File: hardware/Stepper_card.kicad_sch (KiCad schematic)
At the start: 2 parts, among them J3 PCIE-036-02-X-D-TH

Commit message: more routing
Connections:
- net +3V3: now also J3.A11, J3.B11; no longer J3.A12, J3.B12
- net CIPO: now also J3.A5, J3.B5; no longer J3.A3
- net COPI: now also J3.B4
- net SCL: now also J3.B8
- net SCLK: now also J3.A3, J3.B3; no longer J3.A5
- net SDA: now also J3.B7
- net VM: now also J3.A12, J3.B12
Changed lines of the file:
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@@
+	)
+	(junction
+		(at 119.38 104.14)
+		(diameter 0)
+		(color 0 0 0 0)
 	)
 	(junction
@@
 	)
 	(junction
+		(at 163.83 104.14)
+		(diameter 0)
+		(color 0 0 0 0)
+	)
+	(junction
 		(at 172.72 99.06)
 		(diameter 0)
@@
 	(wire
 		(pts
+			(xy 163.83 104.14) (xy 163.83 106.68)
+		)
+		(stroke
+			(width 0)
+			(type default)
+		)
+	)
+	(wire
+		(pts
 			(xy 119.38 114.3) (xy 119.38 116.84)
 		)
@@
 	(wire
 		(pts
+			(xy 157.48 101.6) (xy 196.85 101.6)
+		)
+		(stroke
+			(width 0)
+			(type default)
+		)
+	)
+	(wire
+		(pts
 			(xy 163.83 119.38) (xy 163.83 124.46)
 		)
@@
 	(wire
 		(pts
-			(xy 132.08 104.14) (xy 125.73 104.14)
-		)
-		(stroke
-			(width 0)
-			(type default)
-		)
-	)
-	(wire
-		(pts
 			(xy 132.08 116.84) (xy 119.38 116.84)
 		)
@@
 	(wire
 		(pts
+			(xy 119.38 104.14) (xy 132.08 104.14)
+		)
+		(stroke
+			(width 0)
+			(type default)
+		)
+	)
+	(wire
+		(pts
 			(xy 157.48 83.82) (xy 196.85 83.82)
 		)
@@
 	(wire
 		(pts
-			(xy 157.48 104.14) (xy 196.85 104.14)
-		)
-		(stroke
-			(width 0)
-			(type default)
-		)
-	)
-	(wire
-		(pts
 			(xy 119.38 106.68) (xy 119.38 104.14)
 		)
@@
 	(wire
 		(pts
+			(xy 125.73 81.28) (xy 132.08 81.28)
+		)
+		(stroke
+			(width 0)
+			(type default)
+		)
+	)
+	(wire
+		(pts
 			(xy 196.85 121.92) (xy 181.61 121.92)
 		)
@@
 	(wire
 		(pts
+			(xy 132.08 101.6) (xy 125.73 101.6)
+		)
+		(stroke
+			(width 0)
+			(type default)
+		)
+	)
+	(wire
+		(pts
+			(xy 125.73 83.82) (xy 132.08 83.82)
+		)
+		(stroke
+			(width 0)
+			(type default)
+		)
+	)
+	(wire
+		(pts
 			(xy 157.48 78.74) (xy 196.85 78.74)
 		)
@@
 	(wire
 		(pts
+			(xy 119.38 104.14) (xy 119.38 101.6)
+		)
+		(stroke
+			(width 0)
+			(type default)
+		)
+	)
+	(wire
+		(pts
 			(xy 157.48 91.44) (xy 196.85 91.44)
 		)
@@
 	(wire
 		(pts
-			(xy 163.83 106.68) (xy 196.85 106.68)
+			(xy 163.83 104.14) (xy 196.85 104.14)
+		)
+		(stroke
+			(width 0)
+			(type default)
+		)
+	)
+	(wire
+		(pts
+			(xy 157.48 104.14) (xy 163.83 104.14)
 		)
 		(stroke
@@
 	(wire
 		(pts
+			(xy 125.73 93.98) (xy 132.08 93.98)
+		)
+		(stroke
+			(width 0)
+			(type default)
+		)
+	)
+	(wire
+		(pts
+			(xy 125.73 91.44) (xy 132.08 91.44)
+		)
+		(stroke
+			(width 0)
+			(type default)
+		)
+	)
+	(wire
+		(pts
 			(xy 172.72 99.06) (xy 172.72 110.49)
 		)
@@
 			(width 0)
 			(type default)
+		)
+	)
+	(wire
+		(pts
+			(xy 125.73 86.36) (xy 132.08 86.36)
+		)
+		(stroke
+			(width 0)
+			(type default)
+		)
+	)
+	(label "SCLK"
+		(at 163.83 81.28 180)
+		(effects
+			(font
+				(size 1.27 1.27)
+			)
+			(justify right bottom)
+		)
+	)
+	(label "SCLK"
+		(at 125.73 81.28 0)
+		(effects
+			(font
+				(size 1.27 1.27)
+			)
+			(justify left bottom)
+		)
+	)
+	(label "CIPO"
+		(at 125.73 86.36 0)
+		(effects
+			(font
+				(size 1.27 1.27)
+			)
+			(justify left bottom)
+		)
+	)
+	(label "SCL"
+		(at 125.73 93.98 0)
+		(effects
+			(font
+				(size 1.27 1.27)
+			)
+			(justify left bottom)
+		)
+	)
+	(label "COPI"
+		(at 125.73 83.82 0)
+		(effects
+			(font
+				(size 1.27 1.27)
+			)
+			(justify left bottom)
 		)
 	)
@@
 		)
 	)
-	(label "CIPO"
-		(at 163.83 81.28 180)
-		(effects
-			(font
-				(size 1.27 1.27)
-			)
-			(justify right bottom)
-		)
-	)
 	(label "DIR"
 		(at 163.83 78.74 180)
@@
 		)
 	)
+	(label "SDA"
+		(at 125.73 91.44 0)
+		(effects
+			(font
+				(size 1.27 1.27)
+			)
+			(justify left bottom)
+		)
+	)
 	(label "VM"
-		(at 163.83 106.68 180)
+		(at 163.83 104.14 180)
 		(effects
 			(font
@@
 		)
 	)
-	(label "SCLK"
-		(at 163.83 86.36 180)
-		(effects
-			(font
-				(size 1.27 1.27)
-			)
-			(justify right bottom)
-		)
-	)
 	(label "STEP"
 		(at 163.83 76.2 180)
@@
 	)
 	(label "+3V3"
-		(at 163.83 104.14 180)
+		(at 163.83 101.6 180)
 		(effects
 			(font
@@
 		)
 	)
-	(hierarchical_label "CIPO"
-		(shape input)
-		(at 196.85 81.28 0)
-		(effects
-			(font
-				(size 1.27 1.27)
-			)
-			(justify left)
+	(label "CIPO"
+		(at 163.83 86.36 180)
+		(effects
+			(font
+				(size 1.27 1.27)
+			)
+			(justify right bottom)
 		)
 	)
@@
 	(hierarchical_label "SCLK"
 		(shape input)
+		(at 196.85 81.28 0)
+		(effects
+			(font
+				(size 1.27 1.27)
+			)
+			(justify left)
+		)
+	)
+	(hierarchical_label "CIPO"
+		(shape input)
 		(at 196.85 86.36 0)
 		(effects
@@
 		)
 	)
-	(hierarchical_label "+3V3"
-		(shape input)
-		(at 196.85 104.14 0)
-		(effects
-			(font
-				(size 1.27 1.27)
-			)
-			(justify left)
-		)
-	)
 	(hierarchical_label "GND"
 		(shape input)
@@
 		)
 	)
+	(hierarchical_label "+3V3"
+		(shape input)
+		(at 196.85 101.6 0)
+		(effects
+			(font
+				(size 1.27 1.27)
+			)
+			(justify left)
+		)
+	)
 	(hierarchical_label "VM"
 		(shape input)
-		(at 196.85 106.68 0)
+		(at 196.85 104.14 0)
 		(effects
 			(font
@@
 	(symbol
 		(lib_id "power:+3V3")
-		(at 119.38 104.14 0)
+		(at 119.38 101.6 0)
 		(mirror y)
 		(unit 1)
@@
 		(fields_autoplaced yes)
 		(property "Reference" "#PWR022"
-			(at 119.38 107.95 0)
+			(at 119.38 105.41 0)
 			(effects
 				(font
@@
 		)
 		(property "Value" "VM"
-			(at 119.38 99.06 0)
+			(at 119.38 96.52 0)
 			(effects
 				(font
@@
 		)
 		(property "Footprint" ""
-			(at 119.38 104.14 0)
+			(at 119.38 101.6 0)
 			(effects
 				(font
@@
 		)
 		(property "Datasheet" ""
-			(at 119.38 104.14 0)
+			(at 119.38 101.6 0)
 			(effects
 				(font
@@
 		)
 		(property "Description" "Power symbol creates a global label with name \"+3V3\""
-			(at 119.38 104.14 0)
+			(at 119.38 101.6 0)
 			(effects
 				(font
@@
 	(symbol
 		(lib_id "power:+3V3")
-		(at 125.73 104.14 0)
+		(at 125.73 101.6 0)
 		(mirror y)
 		(unit 1)
@@
 		(fields_autoplaced yes)
 		(property "Reference" "#PWR024"
-			(at 125.73 107.95 0)
+			(at 125.73 105.41 0)
 			(effects
 				(font
@@
 		)
 		(property "Value" "+3V3"
-			(at 125.73 99.06 0)
+			(at 125.73 96.52 0)
 			(effects
 				(font
@@
 		)
 		(property "Footprint" ""
-			(at 125.73 104.14 0)
+			(at 125.73 101.6 0)
 			(effects
 				(font
@@
 		)
 		(property "Datasheet" ""
-			(at 125.73 104.14 0)
+			(at 125.73 101.6 0)
 			(effects
 				(font
@@
 		)
 		(property "Description" "Power symbol creates a global label with name \"+3V3\""
-			(at 125.73 104.14 0)
+			(at 125.73 101.6 0)
 			(effects
 				(font
@@
 			(project "BREAD_Slice"
 				(path "/66043bca-a260-4915-9fce-8a51d324c687/d8306a08-064c-4eaa-a20b-e93bd3d278a4"
-					(reference "#PWR045")
+					(reference "#PWR0103")
 					(unit 1)
 				)
@@
 				)
 				(path "/66043bca-a260-4915-9fce-8a51d324c687/f5513ef3-0e61-46f0-9947-38308ddef54a"
-					(reference "#PWR031")
+					(reference "#PWR0101")
 					(unit 1)
 				)
 				(path "/66043bca-a260-4915-9fce-8a51d324c687/f619a8b7-4532-47fb-ad5f-06ccb6ce9665"
-					(reference "#PWR038")
-					(unit 1)
-				)
+					(reference "#PWR0102")
+					(unit 1)
+				)

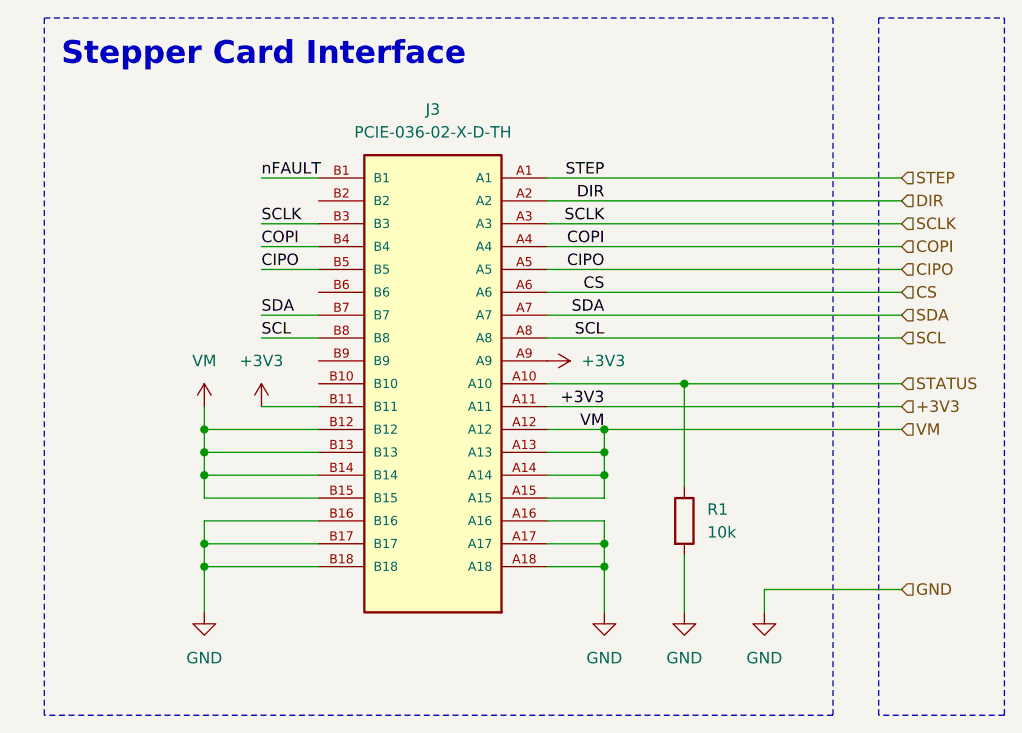
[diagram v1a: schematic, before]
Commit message: finished initial routing
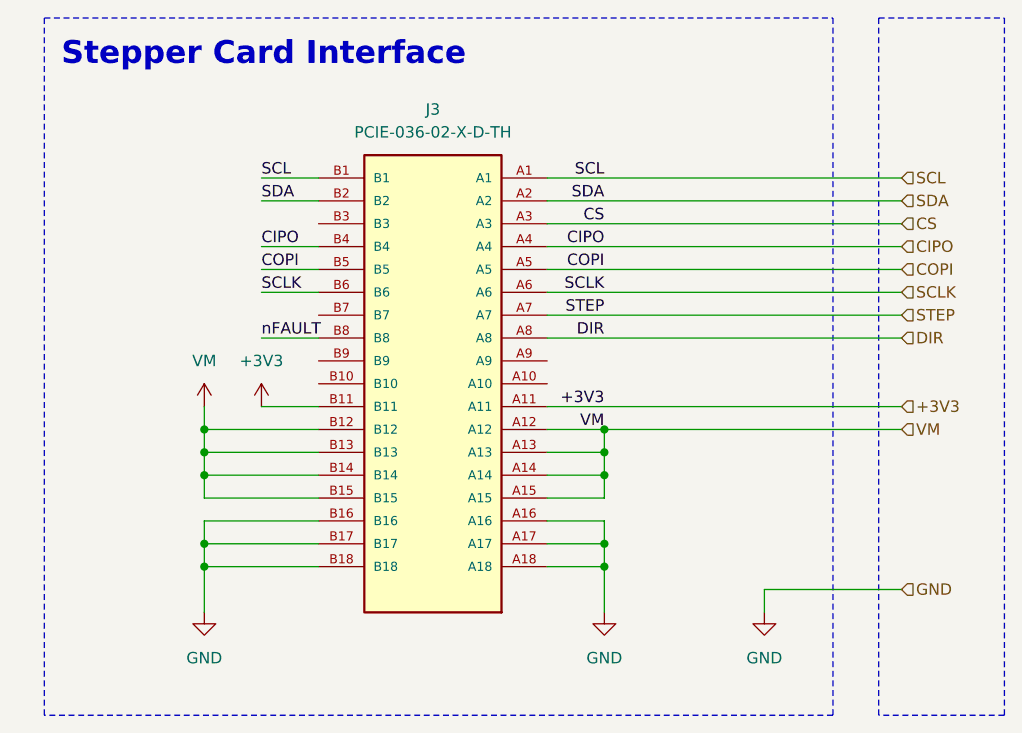
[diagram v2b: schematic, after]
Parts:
- removed R1: 10k, Resistor_SMD:R_0603_1608Metric_Pad0.98x0.95mm_HandSolder, symbol Device:R
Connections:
- net +3V3: no longer J3.A9
- net CIPO: now also J3.A4, J3.B4; no longer J3.A5, J3.B5
- net COPI: now also J3.A5, J3.B5; no longer J3.A4, J3.B4
- net CS: now also J3.A3; no longer J3.A6
- net DIR: now also J3.A8; no longer J3.A2
- net SCL: now also J3.A1, J3.B1; no longer J3.A8, J3.B8
- net SCLK: now also J3.A6, J3.B6; no longer J3.A3, J3.B3
- net SDA: now also J3.A2, J3.B2; no longer J3.A7, J3.B7
- net STEP: now also J3.A7; no longer J3.A1
- net nFAULT: now also J3.B8; no longer J3.B1
- net STATUS: no longer names the net of J3.A10

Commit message: added nFAULT line
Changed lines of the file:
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@@
+	(wire
+		(pts
+			(xy 180.34 96.52) (xy 196.85 96.52)
+		)
+		(stroke
+			(width 0)
+			(type default)
+		)
+	)
 	(wire
 		(pts
@@
 		)
 	)
+	(label "nFAULT"
+		(at 180.34 96.52 0)
+		(effects
+			(font
+				(size 1.27 1.27)
+			)
+			(justify left bottom)
+		)
+	)
 	(label "CS"
 		(at 163.83 81.28 180)
@@
 		(effects
 			(font
+				(size 1.27 1.27)
+			)
+			(justify left)
+		)
+	)
+	(hierarchical_label "nFAULT"
+		(shape input)
+		(at 196.85 96.52 0)
+		(effects
+			(font
